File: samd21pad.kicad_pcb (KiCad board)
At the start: 2 copper layers, 57.8 x 57.9 mm, 26 parts, among them J1 USB_C_Receptacle_USB2.0, J2 Conn_ARM_SWD_TagConnect_TC203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, SW1 SW_Push, SW10 SW_Push, SW2 SW_Push, SW3 SW_Push, SW4 SW_Push, SW5 SW_Push, SW6 SW_Push, SW7 SW_Push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

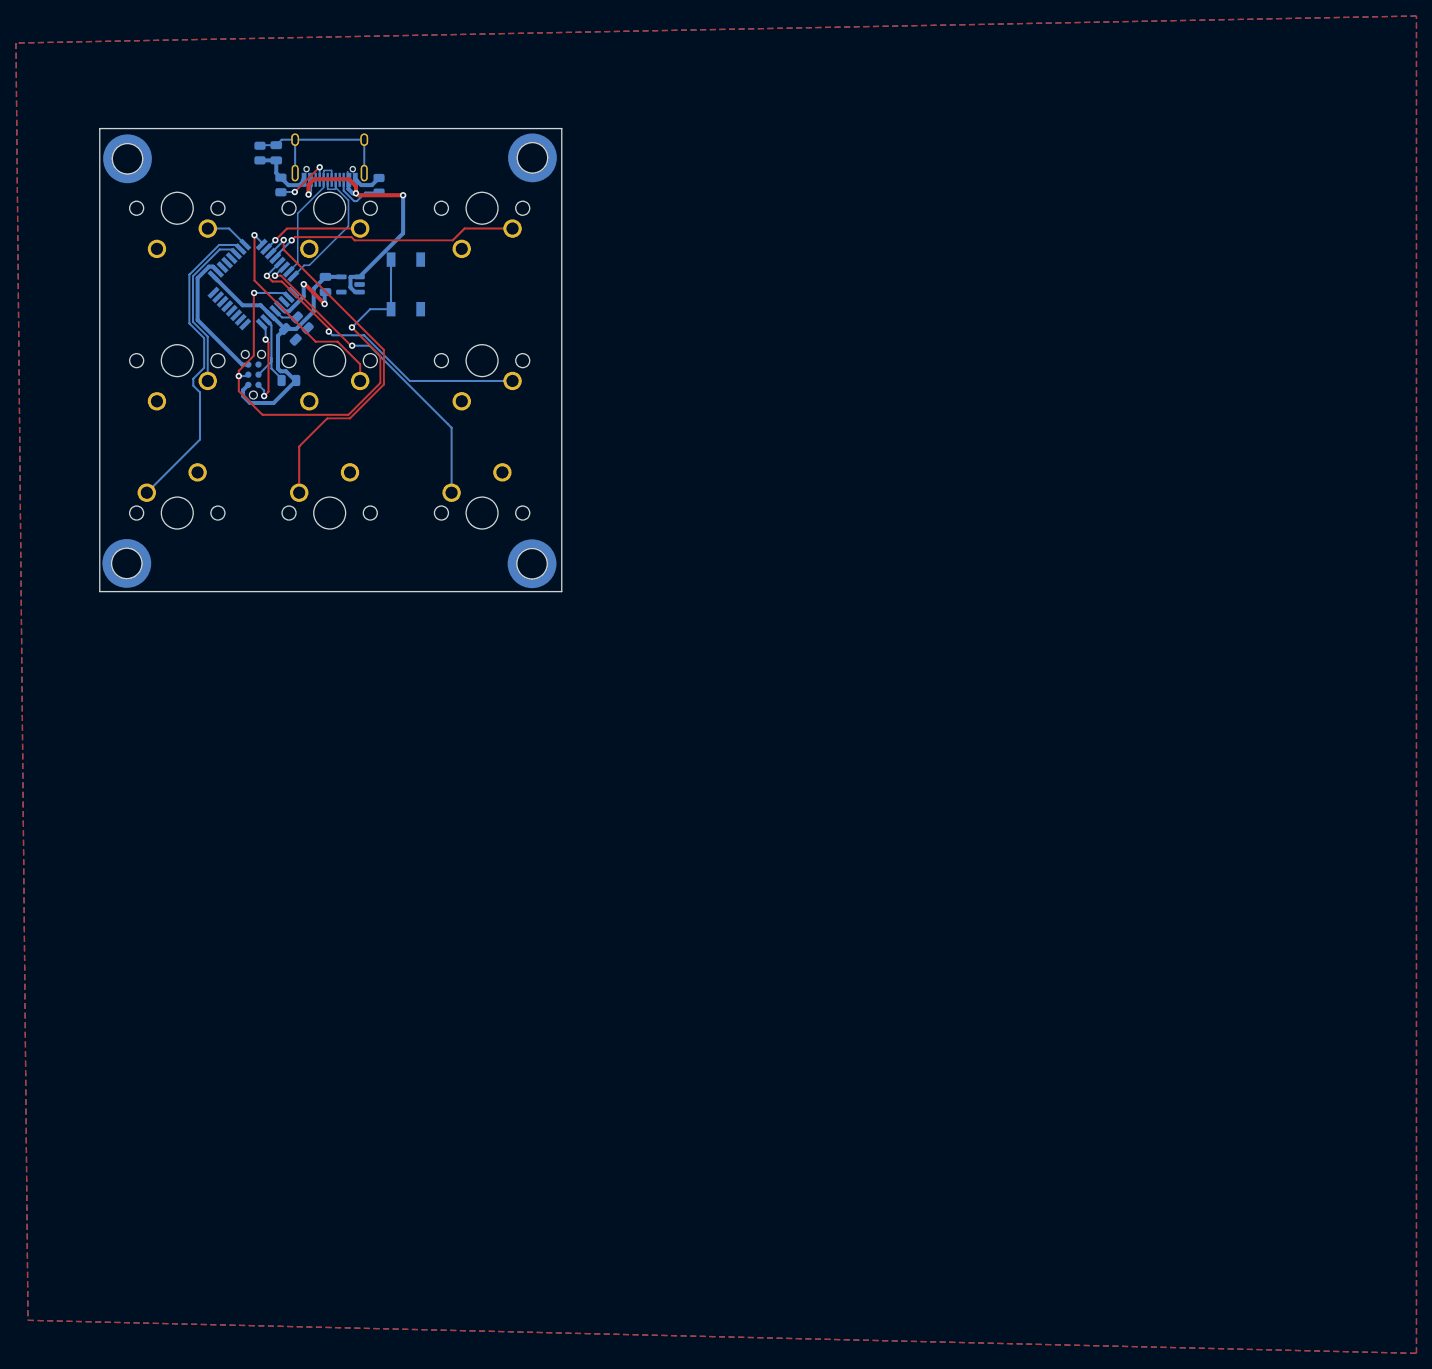
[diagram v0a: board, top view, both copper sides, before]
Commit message: 3-piece assembly edge cuts, mounting holes, plate, and silk fixes.
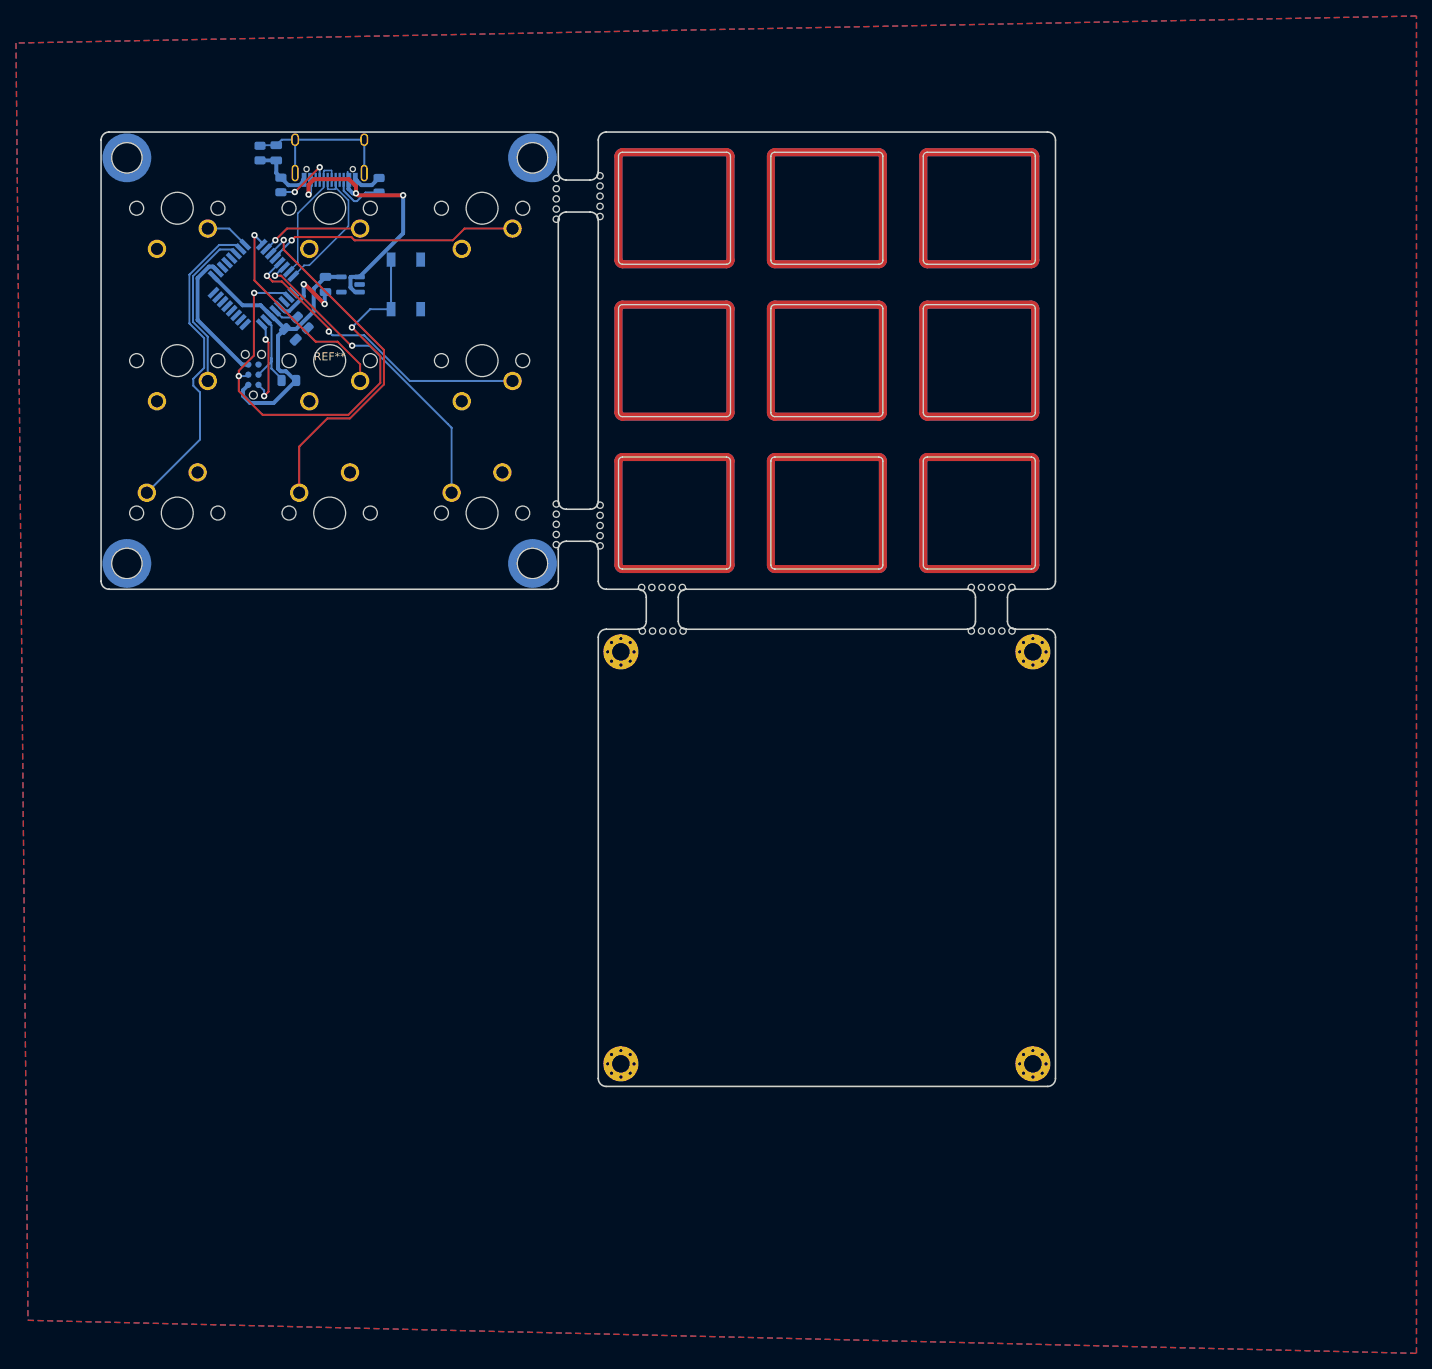
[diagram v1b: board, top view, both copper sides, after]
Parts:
- added REF**: Plate-MP_MX_1u, PCM_marbastlib-xp-plate-mx:Plate-MP_MX_1u, F.Cu at (112.7, 58.0)
- added REF**: MountingHole_2.2mm_M2_Pad_Via, MountingHole:MountingHole_2.2mm_M2_Pad_Via, F.Cu at (106.0, 145.9)
- added REF**: Plate-MP_MX_1u, PCM_marbastlib-xp-plate-mx:Plate-MP_MX_1u, F.Cu at (131.8, 58.0)
- added REF**: Plate-MP_MX_1u, PCM_marbastlib-xp-plate-mx:Plate-MP_MX_1u, F.Cu at (112.7, 39.0)
- added REF**: breakaway-mousebites, samd21pad:breakaway-mousebites, F.Cu at (152.4, 86.6)
- added REF**: breakaway-mousebites, samd21pad:breakaway-mousebites, F.Cu at (103.2, 37.4)
- added REF**: Plate-MP_MX_1u, PCM_marbastlib-xp-plate-mx:Plate-MP_MX_1u, F.Cu at (150.8, 58.0)
- added REF**: MountingHole_2.2mm_M2_Pad_Via, MountingHole:MountingHole_2.2mm_M2_Pad_Via, F.Cu at (157.5, 145.9)
- added REF**: Plate-MP_MX_1u, PCM_marbastlib-xp-plate-mx:Plate-MP_MX_1u, F.Cu at (131.8, 39.0)
- added REF**: breakaway-mousebites, samd21pad:breakaway-mousebites, F.Cu at (152.4, 91.5)
- added REF**: Plate-MP_MX_1u, PCM_marbastlib-xp-plate-mx:Plate-MP_MX_1u, F.Cu at (131.8, 77.0)
- added REF**: Plate-MP_MX_1u, PCM_marbastlib-xp-plate-mx:Plate-MP_MX_1u, F.Cu at (150.8, 39.0)
- added REF**: breakaway-mousebites, samd21pad:breakaway-mousebites, F.Cu at (98.2, 37.8)
- added REF**: MountingHole_2.2mm_M2_Pad_Via, MountingHole:MountingHole_2.2mm_M2_Pad_Via, F.Cu at (157.5, 94.4)
- added REF**: Plate-MP_MX_1u, PCM_marbastlib-xp-plate-mx:Plate-MP_MX_1u, F.Cu at (112.7, 77.0)
- added REF**: Plate-MP_MX_1u, PCM_marbastlib-xp-plate-mx:Plate-MP_MX_1u, F.Cu at (150.8, 77.0)
- added REF**: MountingHole_2.2mm_M2_Pad_Via, MountingHole:MountingHole_2.2mm_M2_Pad_Via, F.Cu at (106.0, 94.4)
- added REF**: breakaway-mousebites, samd21pad:breakaway-mousebites, F.Cu at (98.2, 78.5)
- added REF**: breakaway-mousebites, samd21pad:breakaway-mousebites, F.Cu at (111.3, 91.5)
- added REF**: samd21pad_edge_cuts, samd21pad:samd21pad_edge_cuts, F.Cu at (69.6, 58.0)
- added REF**: breakaway-mousebites, samd21pad:breakaway-mousebites, F.Cu at (103.2, 78.6)
- added REF**: breakaway-mousebites, samd21pad:breakaway-mousebites, F.Cu at (111.2, 86.6)
- H1, H2, H3, H4: renamed from REF**; value MountingHole_3mm_Pad_NonPTH_TopOnly -> MountingHole
- moved H1 0.14 mm to (44.3, 32.6)
- moved H4 0.06 mm to (95.0, 83.3)
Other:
- board size 57.8 x 57.9 mm -> 119.3 x 119.3 mm

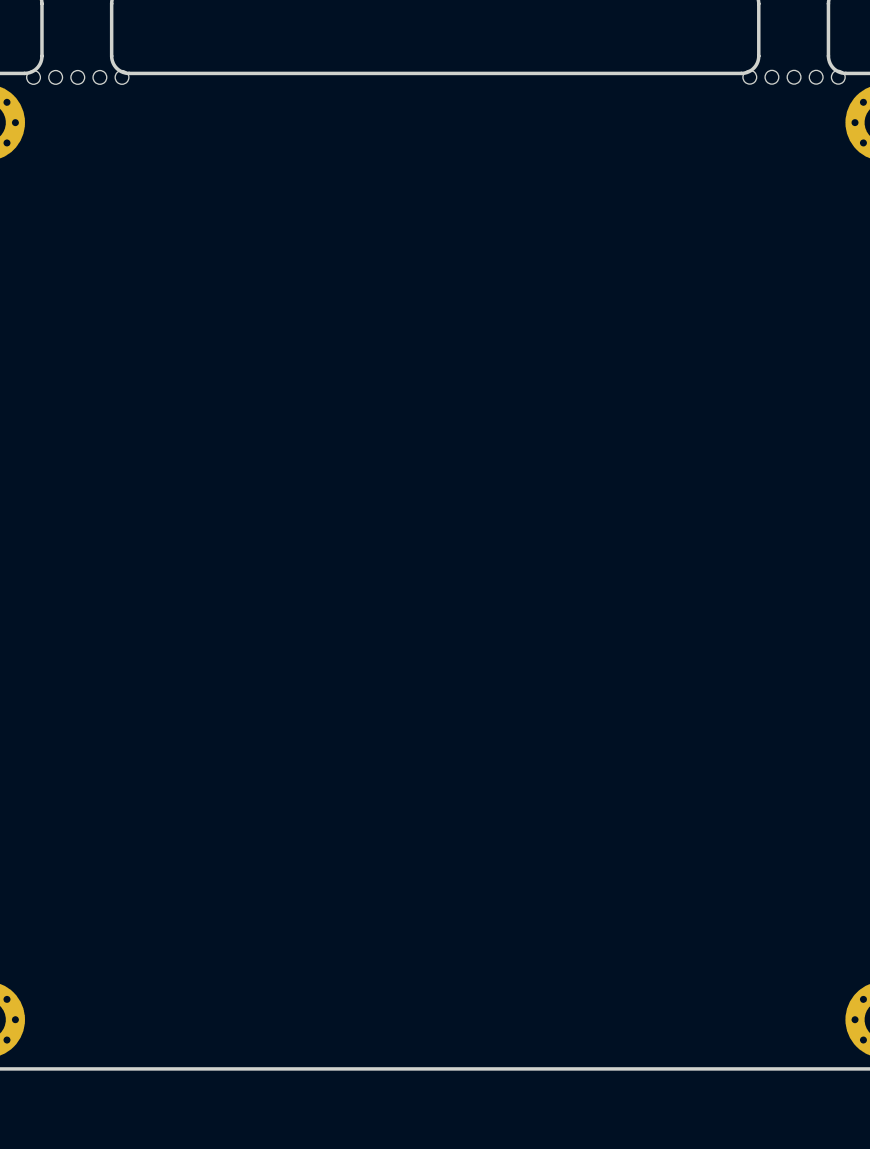
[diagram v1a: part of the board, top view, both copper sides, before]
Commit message: Add silk for the bottom plate for the SMK meetup.
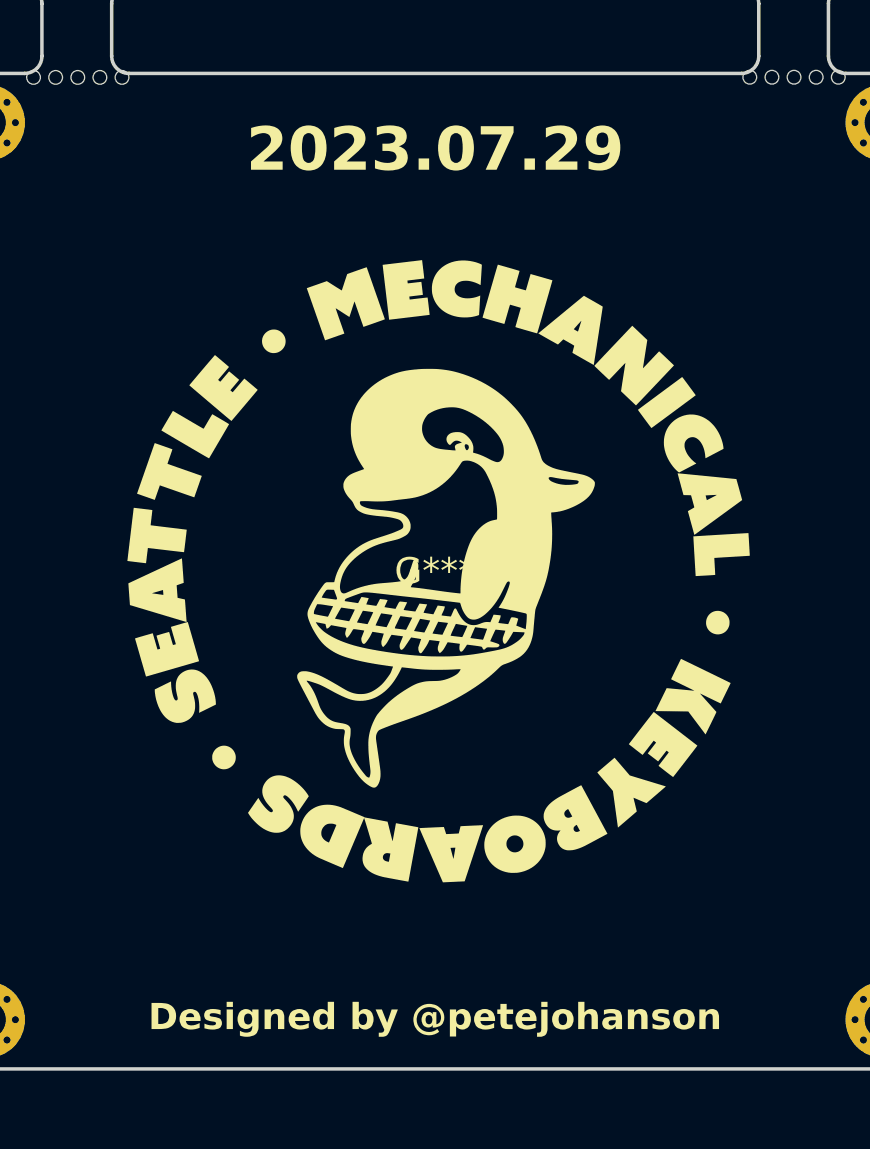
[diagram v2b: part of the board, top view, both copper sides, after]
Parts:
- added G***: LOGO, samd21pad:smk-logo-40x40, F.Cu at (131.8, 120.2)
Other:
- board text added: "2023.07.29"
- board text added: "Designed by @petejohanson"

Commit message: General routing clean ups, silk tweaks, etc.
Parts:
- H1, H2, H3, H4: value MountingHole -> SMTSO2030
- SW10: value SW_Push -> SKQGAKE020
- renumbered SW4 to SW2, SW7 to SW3, SW2 to SW4, SW8 to SW6, SW3 to SW7, SW6 to SW8
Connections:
- SW2 pad 1: SW5 -> SW2
- SW3 pad 1: SW7 -> SW3
- SW4 pad 1: SW2 -> SW4
- SW5 pad 1: SW4 -> SW5
- SW6 pad 1: SW8 -> SW6
- SW7 pad 1: SW3 -> SW7
- SW8 pad 1: SW6 -> SW8
- U1 pad 14: SW2 -> SW4
- U1 pad 15: SW3 -> SW7
- U1 pad 17: SW4 -> SW2
- U1 pad 18: SW5 -> SW3
- U1 pad 19: SW6 -> SW8
- U1 pad 20: SW7 -> SW5
- U1 pad 21: SW8 -> SW9
- U1 pad 22: SW9 -> SW6
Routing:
- net RESET: track 59.9 -> 44.0 mm
- net SW5: track 12.8 -> 22.5 mm
- net SW6: track 45.2 -> 36.7 mm
- net SW7: track 31.6 -> 39.9 mm, vias 1 -> 0
- net SW2: track 20.9 -> 13.0 mm, vias 0 -> 1
- net SW3: track 39.9 -> 32.7 mm, vias 0 -> 1
- net SW4: track 26.8 -> 20.9 mm, vias 1 -> 0
- net +5V: track 36.2 -> 30.9 mm
- net SW9: track 39.7 -> 42.0 mm, vias 2 -> 1
- net SW8: track 38.7 -> 37.0 mm, vias 2 -> 1
- net D+: track 19.3 -> 18.3 mm

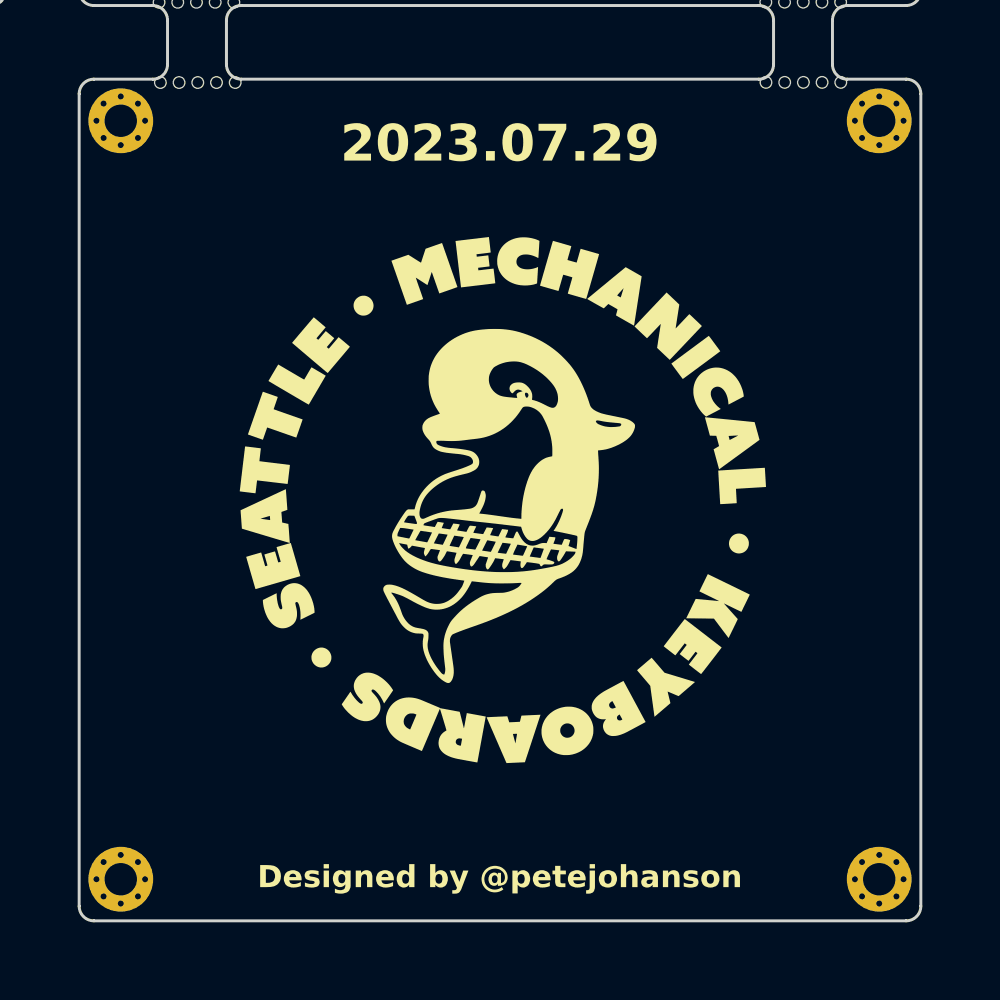
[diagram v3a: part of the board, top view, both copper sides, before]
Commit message: Fix the bottom plate hole locations to align with solder nuts.
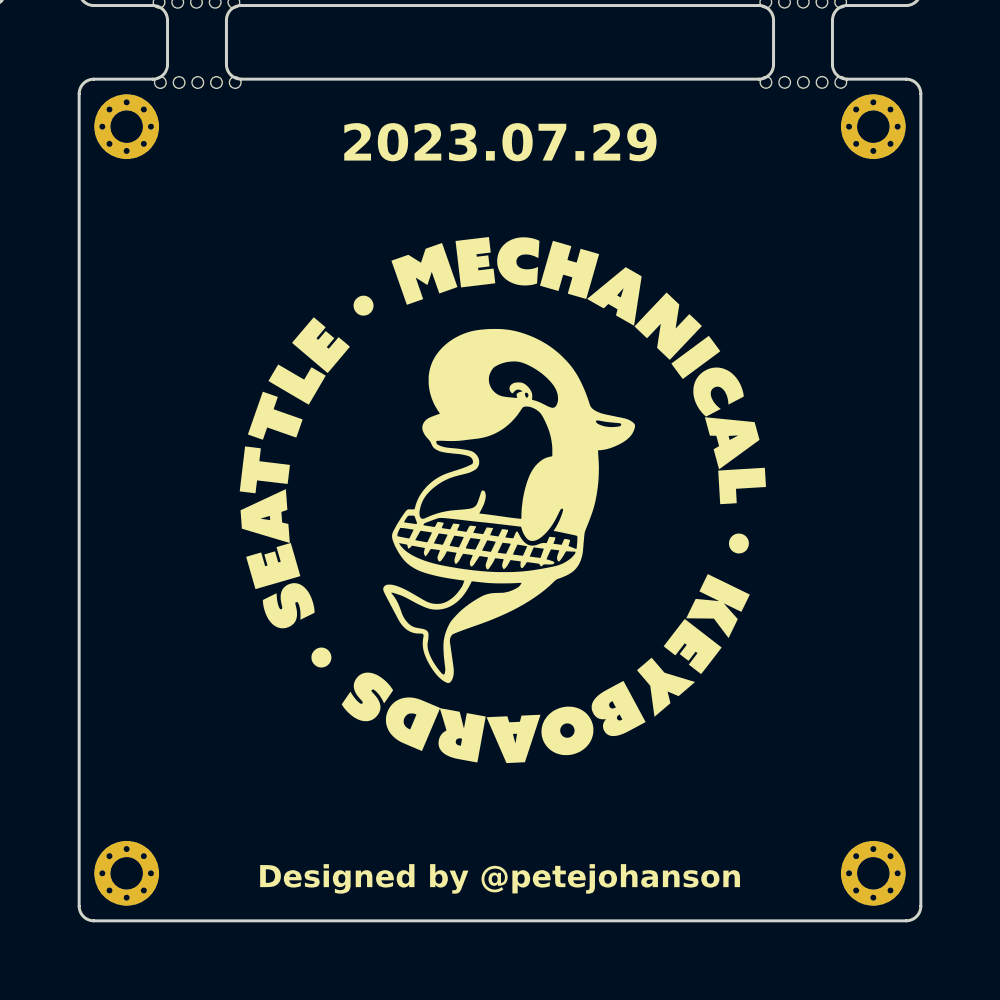
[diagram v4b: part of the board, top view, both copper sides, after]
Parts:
- moved REF** 0.57 mm to (106.4, 145.5)
- moved REF** 0.57 mm to (157.1, 145.5)
- moved REF** 0.57 mm to (157.1, 94.8)
- moved REF** 0.57 mm to (106.4, 94.8)
